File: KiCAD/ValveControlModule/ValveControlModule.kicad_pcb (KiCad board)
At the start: 2 copper layers, 90 x 70 mm, 24 parts, among them J1 DF51A-4P-2DS, J2 DF11-8DP-2DS, U1 XIAO-RP2040-DIP, U2 LT1785xS8, U3 MCP2515-xSO, U4 MCP2562-E-SN, U5 NCV8114BSN330T1G, Y1 8MHz

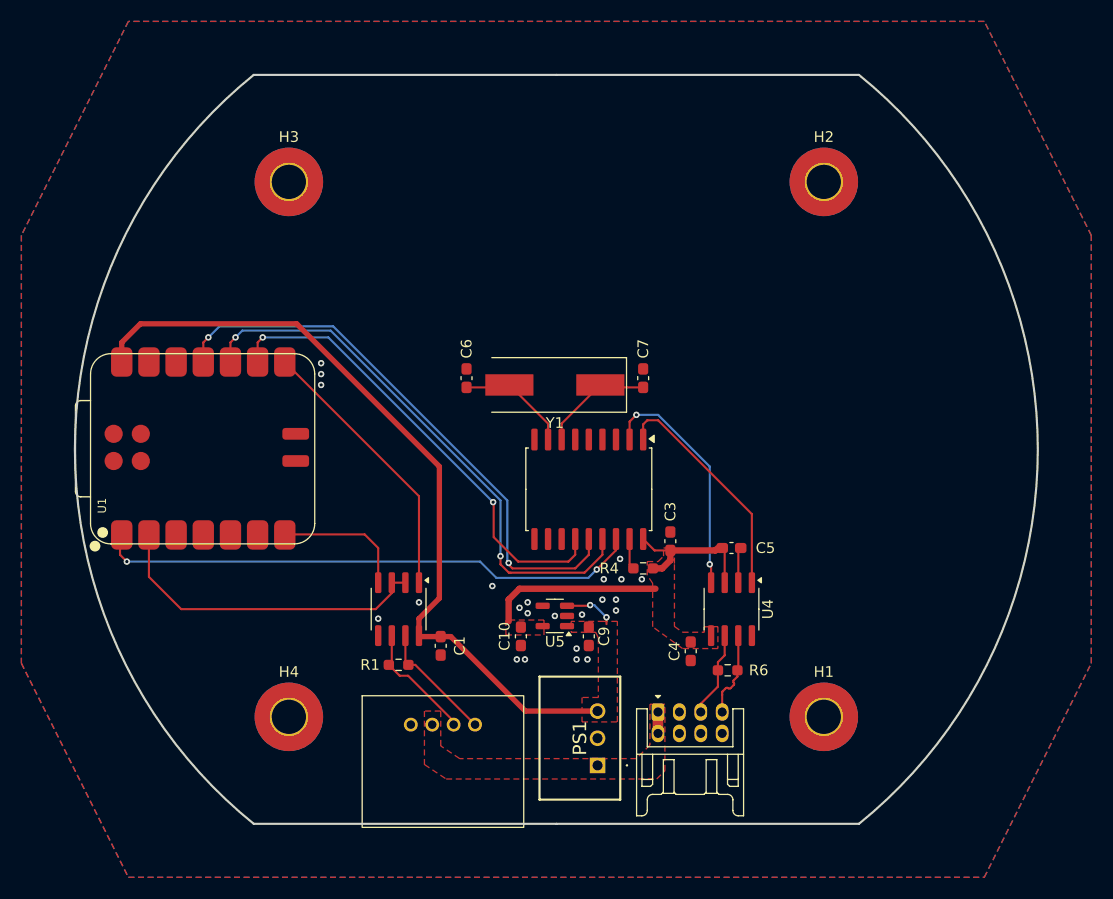
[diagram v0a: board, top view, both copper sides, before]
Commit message: 取り付け穴位置を更新
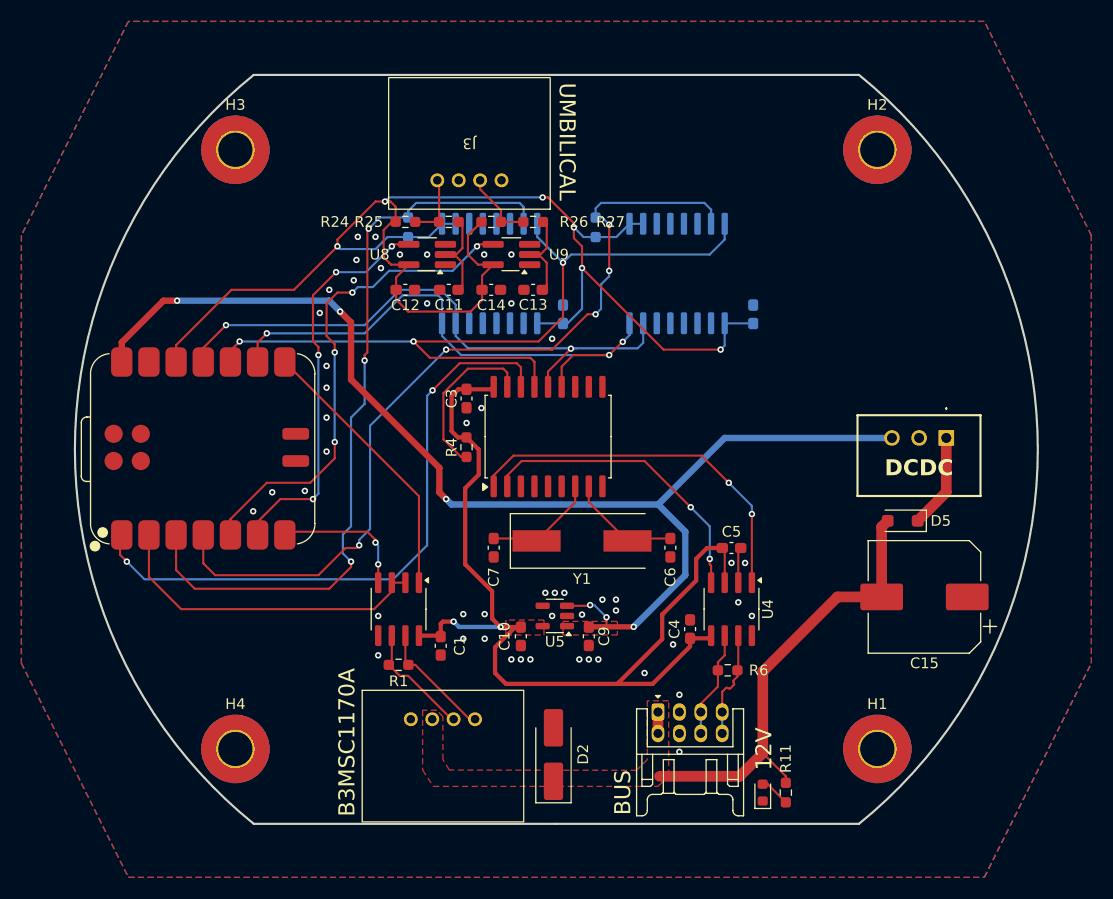
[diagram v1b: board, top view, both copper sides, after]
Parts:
- added 12V: Green, LED_SMD:LED_0603_1608Metric, F.Cu at (169.3, 132.1)
- added C11: 0.1uF, Capacitor_SMD:C_0603_1608Metric_Pad1.08x0.95mm_HandSolder, F.Cu at (140.0, 85.1)
- added C12: 0.1uF, Capacitor_SMD:C_0603_1608Metric_Pad1.08x0.95mm_HandSolder, F.Cu at (135.9, 85.1)
- added C13: 0.1uF, Capacitor_SMD:C_0603_1608Metric_Pad1.08x0.95mm_HandSolder, F.Cu at (147.8, 85.1)
- added C14: 0.1uF, Capacitor_SMD:C_0603_1608Metric_Pad1.08x0.95mm_HandSolder, F.Cu at (143.9, 85.1)
- added C15: 330uF, Capacitor_SMD:CP_Elec_10x10, F.Cu at (184.4, 113.8)
- added C18: 0.1uF, Capacitor_SMD:C_0603_1608Metric_Pad1.08x0.95mm_HandSolder, B.Cu at (168.4, 87.4)
- added C19: 0.1uF, Capacitor_SMD:C_0603_1608Metric_Pad1.08x0.95mm_HandSolder, B.Cu at (150.6, 87.4)
- added D2: SB34AFC, Diode_SMD:D_SMA_Handsoldering, F.Cu at (149.7, 128.5)
- added D5: GS1010FL, Diode_SMD:D_SOD-123F, F.Cu at (182.4, 106.7)
- added G***: LOGO, LOGO, B.Cu at (161.8, 131.3)
- added G***: LOGO, LOGO, B.Cu at (131.5, 131.9)
- added J3: DF51A-4P-2DS, TSRP_Connector_Hirose:DF51A-4P-2DS, F.Cu at (141.9, 65.4)
- added R10: 4.7k, Resistor_SMD:R_0603_1608Metric_Pad0.98x0.95mm_HandSolder, B.Cu at (153.7, 79.2)
- added R11: 2.4kR, Resistor_SMD:R_0603_1608Metric_Pad0.98x0.95mm_HandSolder, F.Cu at (171.4, 132.1)
- added R24: 10kR, Resistor_SMD:R_0603_1608Metric_Pad0.98x0.95mm_HandSolder, F.Cu at (135.9, 78.7)
- added R25: 10kR, Resistor_SMD:R_0603_1608Metric_Pad0.98x0.95mm_HandSolder, F.Cu at (140.0, 78.7)
- added R26: 10kR, Resistor_SMD:R_0603_1608Metric_Pad0.98x0.95mm_HandSolder, F.Cu at (143.9, 78.7)
- added R27: 10kR, Resistor_SMD:R_0603_1608Metric_Pad0.98x0.95mm_HandSolder, F.Cu at (147.8, 78.7)
- added R9: 4.7k, Resistor_SMD:R_0603_1608Metric_Pad0.98x0.95mm_HandSolder, B.Cu at (136.1, 79.2)
- added U6: MB85RQ8MX, Package_SO:SOIC-16W_7.5x10.3mm_P1.27mm, B.Cu at (143.8, 83.6)
- added U7: MB85RQ8MX, Package_SO:SOIC-16W_7.5x10.3mm_P1.27mm, B.Cu at (161.3, 83.6)
- added U8: TC7S14F, Package_TO_SOT_SMD:TSOT-23-5_HandSoldering, F.Cu at (137.9, 81.8)
- added U9: TC7S14F, Package_TO_SOT_SMD:TSOT-23-5_HandSoldering, F.Cu at (145.8, 81.8)
- C1: value 0.1u -> 0.1uF
- C10, C9: value 1u -> 1uF
- moved PS1 44.7 mm to (186.4, 98.9), turned to 180 degrees
- moved C6 24.8 mm to (160.7, 109.2), turned to -90 degrees
- moved C3 23.3 mm to (141.6, 95.2), turned to -90 degrees
- moved C7 21.1 mm to (144.1, 109.2), turned to -90 degrees
- moved R4 20.0 mm to (141.6, 99.8), turned to 90 degrees
- moved Y1 14.8 mm to (152.4, 108.6), turned to 0 degrees
- moved U3 6.23 mm to (149.2, 98.8), turned to 90 degrees
- moved H3 5.83 mm to (120.0, 72.0)
- moved H4 5.83 mm to (120.0, 128.0)
- moved H1 5.83 mm to (180.0, 128.0)
- moved H2 5.83 mm to (180.0, 72.0)
- moved C4 2.07 mm to (162.5, 116.8), turned to -90 degrees
- moved J1 0.51 mm to (139.4, 134.7)
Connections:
- C1 pad 2: +5V -> +3.3V
- PS1 pad 1: +12V -> Net-(D5-K)
- U1 pad 12: unconnected-(U1-3V3-Pad12) -> +3V3
- U1 pad 3: unconnected-(U1-GPIO28/ADC2/A2-Pad3) -> SPI_~{CS}_FeRAM0
- U1 pad 4: unconnected-(U1-GPIO29/ADC3/A3-Pad4) -> SPI_~{CS}_FeRAM1
- U1 pad 5: unconnected-(U1-GPIO6/SDA-Pad5) -> Umbilical_GseValve
- U1 pad 6: unconnected-(U1-GPIO7/SCL-Pad6) -> Umbilical_GseIgnition
- U2 pad 8: +5V -> +3.3V
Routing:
- net +3V3: track 0.00 -> 131.8 mm, vias 0 -> 6
- net SPI_~{CS}_FeRAM1: track 0.00 -> 79.7 mm, vias 0 -> 5
- net SPI_~{CS}_FeRAM0: track 0.00 -> 71.7 mm, vias 0 -> 3
- net +3.3V: track 30.3 -> 89.8 mm, vias 0 -> 2
- net Umbilical_GseValve: track 0.00 -> 46.2 mm, vias 0 -> 4
- net +12V: track 2.00 -> 45.2 mm
- net Umbilical_GseIgnition: track 0.00 -> 37.7 mm, vias 0 -> 4
- net +5V: track 78.8 -> 113.9 mm, vias 2 -> 6
- net SPI_MISO: track 52.1 -> 75.1 mm, vias 2 -> 3
- net CAN_TX: track 21.8 -> 35.0 mm, vias 0 -> 2
- net Net-(U3-~{RESET}): track 2.89 -> 15.6 mm
- net Net-(C13-Pad2): track 0.00 -> 9.06 mm
- net Net-(C11-Pad2): track 0.00 -> 9.06 mm
- net Net-(D5-K): track 0.00 -> 8.85 mm
- net SPI_CS_MCP2515: track 51.3 -> 58.9 mm
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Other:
- board text added: "12V"
- board text added: "B3MSC1170A"
- board text added: "BUS"
- board text added: "DCDC"
- board text added: "SUBARU"
- board text added: "Tokai Student Rocket Project"
- board text added: "UMBILICAL"
- board text added: "V1.3"
- board text added: "Valve Control Module Build-1"

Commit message: 3Dモデルを組み合わせて結合試験する
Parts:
- removed the G*** at (161.8, 131.3)
- removed the G*** at (131.5, 131.9)
- added G***: LOGO, LOGO, B.Cu at (133.1, 131.1)
- added G***: LOGO, LOGO, B.Cu at (164.1, 131.1)
- U2: value LT1785xS8 -> LTC1480
- U5: value NCV8114BSN330T1G -> RT9080-22GJ5

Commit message: ガバーデータ生成
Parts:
- moved J3 6.11 mm to (135.8, 65.3)
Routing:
- net Net-(J3-Pin_2): track 6.78 -> 11.8 mm
- net Net-(J3-Pin_4): track 6.19 -> 7.93 mm
- net +3V3: track 131.8 -> 133.3 mm

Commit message: Build-2完成．発注．
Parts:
- removed C19: 0.1uF, Capacitor_SMD:C_0603_1608Metric_Pad1.08x0.95mm_HandSolder
- removed D2: SB34AFC, Diode_SMD:D_SMA_Handsoldering
- removed D5: GS1010FL, Diode_SMD:D_SOD-123F
- removed U7: MB85RQ8MX, Package_SO:SOIC-16W_7.5x10.3mm_P1.27mm
- added C16: 100uF, Capacitor_THT:CP_Radial_D8.0mm_P3.50mm, F.Cu at (151.3, 123.4)
- added C17: 22uF, Capacitor_SMD:C_0805_2012Metric_Pad1.18x1.45mm_HandSolder, F.Cu at (128.3, 125.0)
- added D1: SMAJ45A, Diode_SMD:D_SMA, F.Cu at (149.1, 130.8)
- added D9: SB34AFC, Diode_SMD:D_SMA_Handsoldering, F.Cu at (185.2, 105.4)
- added Q1: AO3400A, Package_TO_SOT_SMD:SOT-23_Handsoldering, F.Cu at (119.9, 119.4)
- added Q2: AO3401A, Package_TO_SOT_SMD:SOT-23_Handsoldering, F.Cu at (126.0, 121.2)
- added Q4: AO3401A, Package_TO_SOT_SMD:SOT-23_Handsoldering, F.Cu at (129.0, 117.6)
- added R12: 10kR, Resistor_SMD:R_0603_1608Metric_Pad0.98x0.95mm_HandSolder, F.Cu at (124.0, 117.6)
- added R13: 100kR, Resistor_SMD:R_0603_1608Metric_Pad0.98x0.95mm_HandSolder, F.Cu at (118.8, 116.6)
- R10: value 4.7k -> 820R; moved to F.Cu
- U2: value LTC1480 -> LT1785xS8
- U5: value RT9080-22GJ5 -> RT9080-33GJ5
- moved R10 56.4 mm to (115.1, 120.4), turned to 0 degrees
- moved C18 17.5 mm to (150.9, 87.4)
- moved C4 8.90 mm to (170.4, 112.8), turned to 90 degrees
- moved R11 6.60 mm to (168.9, 126.0)
- moved PS1 3.05 mm to (186.4, 95.9)
- moved D3 2.57 mm to (168.9, 129.5)
- moved J3 2.42 mm to (138.2, 65.2)
- moved C5 1.30 mm to (166.1, 108.0)
- turned C15 to 0 degrees
- renumbered 12V to D3
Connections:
- C15 pad 1: GND -> +12V
- C15 pad 2: +12V -> GND
- C4 pad 2: +3.3V -> +5V
- H1 pad 1: GND -> (no net)
- H2 pad 1: GND -> (no net)
- H3 pad 1: GND -> (no net)
- H4 pad 1: GND -> (no net)
- J1 pad 2: +12V -> Net-(J1-Pin_2)
- R10 pad 1: +3V3 -> ServoPower_EN
- R10 pad 2: SPI_~{CS}_FeRAM1 -> Net-(Q1-G)
- U1 pad 4: SPI_~{CS}_FeRAM1 -> ServoPower_EN
- U4 pad 3: +3.3V -> +5V
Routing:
- net SPI_~{CS}_FeRAM1: track 79.7 -> 0.00 mm, vias 5 -> 0
- net +12V: track 45.2 -> 97.0 mm
- net +3V3: track 133.3 -> 104.4 mm, vias 6 -> 4
- net Net-(Q2-G): track 0.00 -> 21.5 mm, vias 0 -> 2
- net SPI_MISO: track 75.1 -> 57.6 mm
- net +5V: track 113.9 -> 128.7 mm, vias 6 -> 8
- net ServoPower_EN: track 0.00 -> 13.6 mm, vias 0 -> 2
- net SPI_MOSI: track 55.7 -> 42.6 mm
- net Net-(J1-Pin_2): track 0.00 -> 12.6 mm
- net SPI_SCK: track 51.4 -> 39.0 mm, vias 3 -> 2
- net +3.3V: track 89.8 -> 79.2 mm
- net Net-(Q1-G): track 0.00 -> 2.44 mm
- net Net-(J3-Pin_2): track 11.8 -> 9.44 mm
- net Net-(Q1-D): track 0.00 -> 2.03 mm
- net Net-(Q2-D): track 0.00 -> 1.61 mm
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- removed copper zone on F.Cu, net +12V
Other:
- board text added: "Valve Control Module Build-2"
- board text removed: "DCDC"
- board text removed: "Valve Control Module Build-1"

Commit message: Build-3発注済み
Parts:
- removed Q1: AO3400A, Package_TO_SOT_SMD:SOT-23_Handsoldering
- added Q3: AO3400A, Package_TO_SOT_SMD:SOT-23_Handsoldering, F.Cu at (117.1, 118.1)
- added R14: 10kR, Resistor_SMD:R_0603_1608Metric_Pad0.98x0.95mm_HandSolder, F.Cu at (112.9, 118.1)
- U5: value RT9080-33GJ5 -> NCV8114BSN330T1G
- Y1: footprint Crystal:Crystal_SMD_HC49-SD -> Crystal:Crystal_HC49-4H_Vertical
- moved R12 10.7 mm to (128.3, 127.4), turned to 180 degrees
- moved R10 5.18 mm to (116.1, 115.3), turned to 180 degrees
- moved Q4 3.76 mm to (128.3, 121.3), turned to 90 degrees
- moved Q2 2.85 mm to (124.5, 118.7), turned to -90 degrees
- moved Y1 2.58 mm to (149.8, 108.8)
- moved R13 2.31 mm to (121.2, 116.7), turned to -90 degrees
- moved C17 0.38 mm to (128.3, 125.3), turned to 180 degrees
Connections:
- Q2 pad 2: Net-(Q2-D) -> Net-(J1-Pin_2)
- Q2 pad 3: +12V -> Net-(Q2-D)
- Q4 pad 2: Net-(Q2-D) -> +12V
- Q4 pad 3: Net-(J1-Pin_2) -> Net-(Q2-D)
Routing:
- net Net-(J1-Pin_2): track 12.6 -> 27.4 mm
- net +12V: track 97.0 -> 91.5 mm
- net ServoPower_EN: track 13.6 -> 8.47 mm
- net Net-(Q3-G): track 2.44 -> 4.73 mm
- net RS485_EN: track 29.9 -> 28.3 mm
- net Net-(Q2-D): track 1.61 -> 0.00 mm
- net OSC1: track 10.7 -> 12.2 mm
- net OSC2: track 10.7 -> 12.1 mm
- net Net-(Q2-G): track 21.5 -> 20.4 mm, vias 2 -> 3
- net Net-(Q3-D): track 2.03 -> 2.76 mm
- net GND: vias 153 -> 156
- added copper zone on F.Cu, net Net-(Q2-D)
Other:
- board text added: "Valve Control Module Build-3"
- board text removed: "Valve Control Module Build-2"
